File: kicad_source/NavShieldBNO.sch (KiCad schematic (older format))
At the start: 3 parts

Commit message: updated schematic, added schematic pdf
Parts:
- added C? (x5): 100nF, capacitors:C_0603, symbol devices:C_0603
- added R? (x11): DNI, resistors:R_0603, symbol devices:R_0603
- added R? (x9): 0R, resistors:R_0603, symbol devices:R_0603
- added R? (x5): 10k, resistors:R_0603, symbol devices:R_0603
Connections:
- net labels added: BNO085_CS, BNO085_INT, BOOTN, CAP, CLKSEL0, CSB, ENV_SCL, ENV_SDA, PS0, PS1, RESET, SCK, SDI, SDO
- wire segments 34 -> 128
- no-connect marks 3 -> 18
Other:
- note added: "i2c address 0x4A or 0x4B"
- note added: "i2c address 0x76 or 0x77"
- note added: "set to SPI"
- note added: "should also support BNO055, BNO070, BNO080 and BNO085\nas all have the same footprint and pin out"
- note added: "use internal clock"
- moved on the sheet: U?

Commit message: annotated schematic
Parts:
- gave numbers to parts that had none: 33

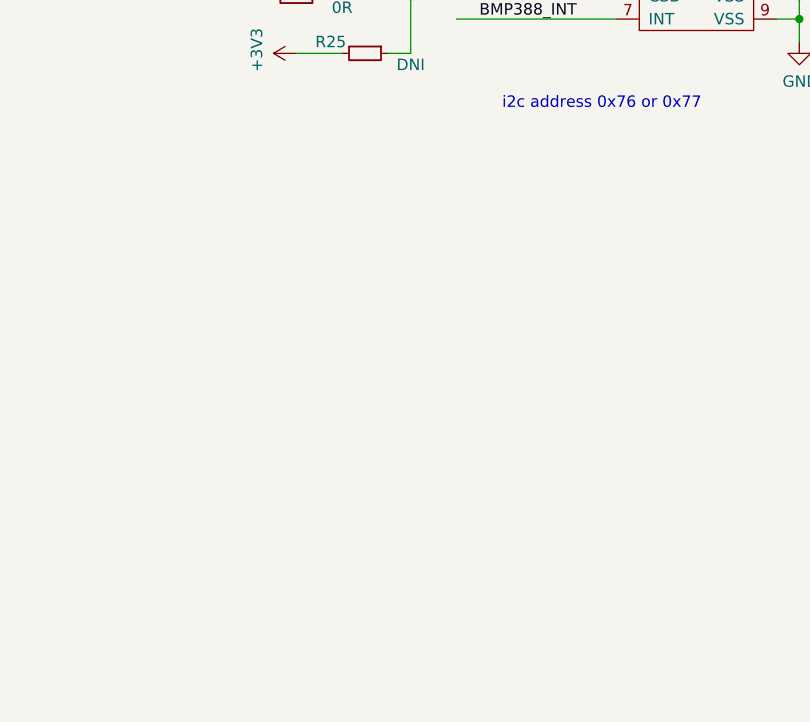
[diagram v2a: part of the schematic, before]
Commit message: added pull up on INT and reset lines
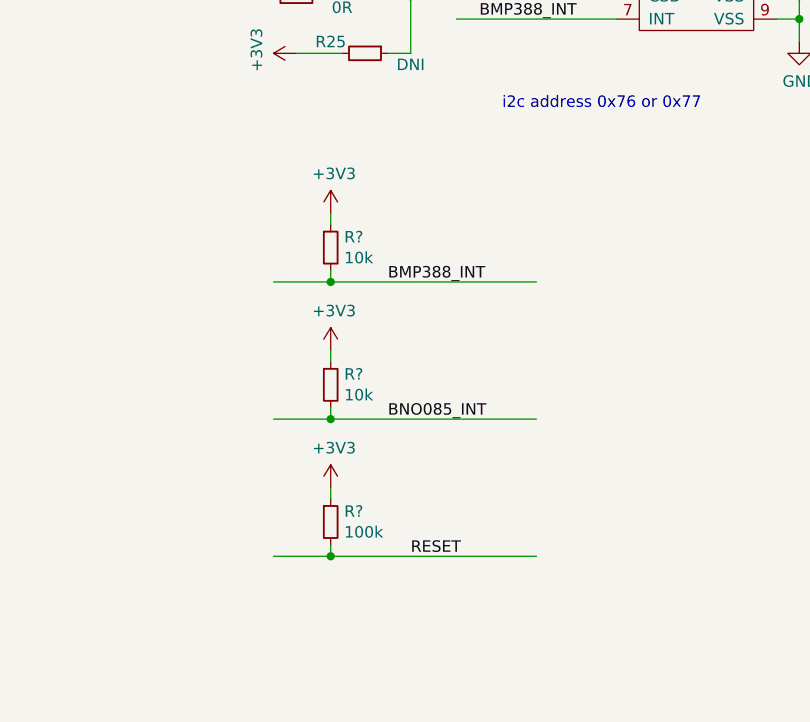
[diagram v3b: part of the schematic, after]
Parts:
- added R? (x2): 10k, resistors:R_0603, symbol devices:R_0603
- added R?: 100k, resistors:R_0603, symbol devices:R_0603
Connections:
- wire segments 128 -> 140
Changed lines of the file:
@@
 Text Notes 1900 700  0    50   ~ 0
 should also support BNO055, BNO070, BNO080 and BNO085\nas all have the same footprint and pin out
+$Comp
+L devices:R_0603 R?
+U 1 1 5F58EB42
+P 8950 3500
+F 0 "R?" H 9009 3546 50  0000 L CNN
+F 1 "10k" H 9009 3455 50  0000 L CNN
+F 2 "resistors:R_0603" H 8950 3350 50  0001 C CNN
+F 3 "" H 8950 3500 50  0000 C CNN
+	1    8950 3500
+	1    0    0    -1
+$EndComp
+$Comp
+L power-supply:+3V3 #PWR?
+U 1 1 5F58EB4C
+P 8950 3350
+F 0 "#PWR?" H 8950 3200 50  0001 C CNN
+F 1 "+3V3" H 8965 3523 50  0000 C CNN
+F 2 "" H 8950 3350 50  0000 C CNN
+F 3 "" H 8950 3350 50  0000 C CNN
+	1    8950 3350
+	1    0    0    -1
+$EndComp
+Wire Wire Line
+	8950 3350 8950 3400
+Wire Wire Line
+	8700 3650 8950 3650
+Wire Wire Line
+	8950 3600 8950 3650
+Connection ~ 8950 3650
+Wire Wire Line
+	8950 3650 9850 3650
+Text Label 9200 3650 0    50   ~ 0
+BMP388_INT
+$Comp
+L devices:R_0603 R?
+U 1 1 5F5A6A36
+P 8950 4100
+F 0 "R?" H 9009 4146 50  0000 L CNN
+F 1 "10k" H 9009 4055 50  0000 L CNN
+F 2 "resistors:R_0603" H 8950 3950 50  0001 C CNN
+F 3 "" H 8950 4100 50  0000 C CNN
+	1    8950 4100
+	1    0    0    -1
+$EndComp
+$Comp
+L power-supply:+3V3 #PWR?
+U 1 1 5F5A6A40
+P 8950 3950
+F 0 "#PWR?" H 8950 3800 50  0001 C CNN
+F 1 "+3V3" H 8965 4123 50  0000 C CNN
+F 2 "" H 8950 3950 50  0000 C CNN
+F 3 "" H 8950 3950 50  0000 C CNN
+	1    8950 3950
+	1    0    0    -1
+$EndComp
+Wire Wire Line
+	8950 3950 8950 4000
+Wire Wire Line
+	8700 4250 8950 4250
+Wire Wire Line
+	8950 4200 8950 4250
+Connection ~ 8950 4250
+Wire Wire Line
+	8950 4250 9850 4250
+Text Label 9200 4250 0    50   ~ 0
+BNO085_INT
+$Comp
+L devices:R_0603 R?
+U 1 1 5F5B49FC
+P 8950 4700
+F 0 "R?" H 9009 4746 50  0000 L CNN
+F 1 "100k" H 9009 4655 50  0000 L CNN
+F 2 "resistors:R_0603" H 8950 4550 50  0001 C CNN
+F 3 "" H 8950 4700 50  0000 C CNN
+	1    8950 4700
+	1    0    0    -1
+$EndComp
+$Comp
+L power-supply:+3V3 #PWR?
+U 1 1 5F5B4A06
+P 8950 4550
+F 0 "#PWR?" H 8950 4400 50  0001 C CNN
+F 1 "+3V3" H 8965 4723 50  0000 C CNN
+F 2 "" H 8950 4550 50  0000 C CNN
+F 3 "" H 8950 4550 50  0000 C CNN
+	1    8950 4550
+	1    0    0    -1
+$EndComp
+Wire Wire Line
+	8950 4550 8950 4600
+Wire Wire Line
+	8700 4850 8950 4850
+Wire Wire Line
+	8950 4800 8950 4850
+Connection ~ 8950 4850
+Wire Wire Line
+	8950 4850 9850 4850
+Text Label 9300 4850 0    50   ~ 0
+RESET
 $EndSCHEMATC

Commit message: connected CLKSEL1 to GND via resistor
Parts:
- added R?: 0R, resistors:R_0603, symbol devices:R_0603
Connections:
- net labels added: CLKSEL1
- wire segments 140 -> 142
- no-connect marks 18 -> 17
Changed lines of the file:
@@
 Text Label 2950 7100 0    50   ~ 0
 BNO085_CS
-NoConn ~ 4150 1800
 NoConn ~ 4150 1300
 Wire Wire Line
@@
 Text Label 9300 4850 0    50   ~ 0
 RESET
+$Comp
+L power-supply:GND #PWR?
+U 1 1 5F5C11F4
+P 4950 1800
+F 0 "#PWR?" H 4950 1550 50  0001 C CNN
+F 1 "GND" H 4955 1627 50  0000 C CNN
+F 2 "" H 4950 1800 50  0000 C CNN
+F 3 "" H 4950 1800 50  0000 C CNN
+	1    4950 1800
+	1    0    0    -1
+$EndComp
+$Comp
+L devices:R_0603 R?
+U 1 1 5F5C376C
+P 4750 1800
+F 0 "R?" H 4809 1846 50  0000 L CNN
+F 1 "0R" H 4809 1755 50  0000 L CNN
+F 2 "resistors:R_0603" H 4750 1650 50  0001 C CNN
+F 3 "" H 4750 1800 50  0000 C CNN
+	1    4750 1800
+	0    -1   -1   0
+$EndComp
+Wire Wire Line
+	4150 1800 4650 1800
+Wire Wire Line
+	4850 1800 4950 1800
+Text Label 4250 1800 0    50   ~ 0
+CLKSEL1
 $EndSCHEMATC

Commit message: moved BNO085_CS to D5, updated schematic pdf
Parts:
- gave numbers to parts that had none: 4
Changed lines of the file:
@@
 Wire Wire Line
 	4150 2750 5650 2750
-Wire Wire Line
-	2800 7100 3650 7100
-Text Label 2950 7100 0    50   ~ 0
+Text Label 2950 7300 0    50   ~ 0
 BNO085_CS
 NoConn ~ 4150 1300
@@
 NoConn ~ 4850 6500
 NoConn ~ 4850 6600
-NoConn ~ 3650 7300
 NoConn ~ 3650 7200
 NoConn ~ 3650 6900
@@
 should also support BNO055, BNO070, BNO080 and BNO085\nas all have the same footprint and pin out
 $Comp
-L devices:R_0603 R?
+L devices:R_0603 R27
 U 1 1 5F58EB42
 P 8950 3500
-F 0 "R?" H 9009 3546 50  0000 L CNN
+F 0 "R27" H 9009 3546 50  0000 L CNN
 F 1 "10k" H 9009 3455 50  0000 L CNN
 F 2 "resistors:R_0603" H 8950 3350 50  0001 C CNN
@@
 $EndComp
 $Comp
-L power-supply:+3V3 #PWR?
+L power-supply:+3V3 #PWR030
 U 1 1 5F58EB4C
 P 8950 3350
-F 0 "#PWR?" H 8950 3200 50  0001 C CNN
+F 0 "#PWR030" H 8950 3200 50  0001 C CNN
 F 1 "+3V3" H 8965 3523 50  0000 C CNN
 F 2 "" H 8950 3350 50  0000 C CNN
@@
 BMP388_INT
 $Comp
-L devices:R_0603 R?
+L devices:R_0603 R28
 U 1 1 5F5A6A36
 P 8950 4100
-F 0 "R?" H 9009 4146 50  0000 L CNN
+F 0 "R28" H 9009 4146 50  0000 L CNN
 F 1 "10k" H 9009 4055 50  0000 L CNN
 F 2 "resistors:R_0603" H 8950 3950 50  0001 C CNN
@@
 $EndComp
 $Comp
-L power-supply:+3V3 #PWR?
+L power-supply:+3V3 #PWR031
 U 1 1 5F5A6A40
 P 8950 3950
-F 0 "#PWR?" H 8950 3800 50  0001 C CNN
+F 0 "#PWR031" H 8950 3800 50  0001 C CNN
 F 1 "+3V3" H 8965 4123 50  0000 C CNN
 F 2 "" H 8950 3950 50  0000 C CNN
@@
 BNO085_INT
 $Comp
-L devices:R_0603 R?
+L devices:R_0603 R29
 U 1 1 5F5B49FC
 P 8950 4700
-F 0 "R?" H 9009 4746 50  0000 L CNN
+F 0 "R29" H 9009 4746 50  0000 L CNN
 F 1 "100k" H 9009 4655 50  0000 L CNN
 F 2 "resistors:R_0603" H 8950 4550 50  0001 C CNN
@@
 $EndComp
 $Comp
-L power-supply:+3V3 #PWR?
+L power-supply:+3V3 #PWR032
 U 1 1 5F5B4A06
 P 8950 4550
-F 0 "#PWR?" H 8950 4400 50  0001 C CNN
+F 0 "#PWR032" H 8950 4400 50  0001 C CNN
 F 1 "+3V3" H 8965 4723 50  0000 C CNN
 F 2 "" H 8950 4550 50  0000 C CNN
@@
 RESET
 $Comp
-L power-supply:GND #PWR?
+L power-supply:GND #PWR029
 U 1 1 5F5C11F4
 P 4950 1800
-F 0 "#PWR?" H 4950 1550 50  0001 C CNN
+F 0 "#PWR029" H 4950 1550 50  0001 C CNN
 F 1 "GND" H 4955 1627 50  0000 C CNN
 F 2 "" H 4950 1800 50  0000 C CNN
@@
 $EndComp
 $Comp
-L devices:R_0603 R?
+L devices:R_0603 R26
 U 1 1 5F5C376C
 P 4750 1800
-F 0 "R?" H 4809 1846 50  0000 L CNN
+F 0 "R26" H 4809 1846 50  0000 L CNN
 F 1 "0R" H 4809 1755 50  0000 L CNN
 F 2 "resistors:R_0603" H 4750 1650 50  0001 C CNN
@@
 Text Label 4250 1800 0    50   ~ 0
 CLKSEL1
+Wire Wire Line
+	2800 7300 3650 7300
+NoConn ~ 3650 7100
 $EndSCHEMATC

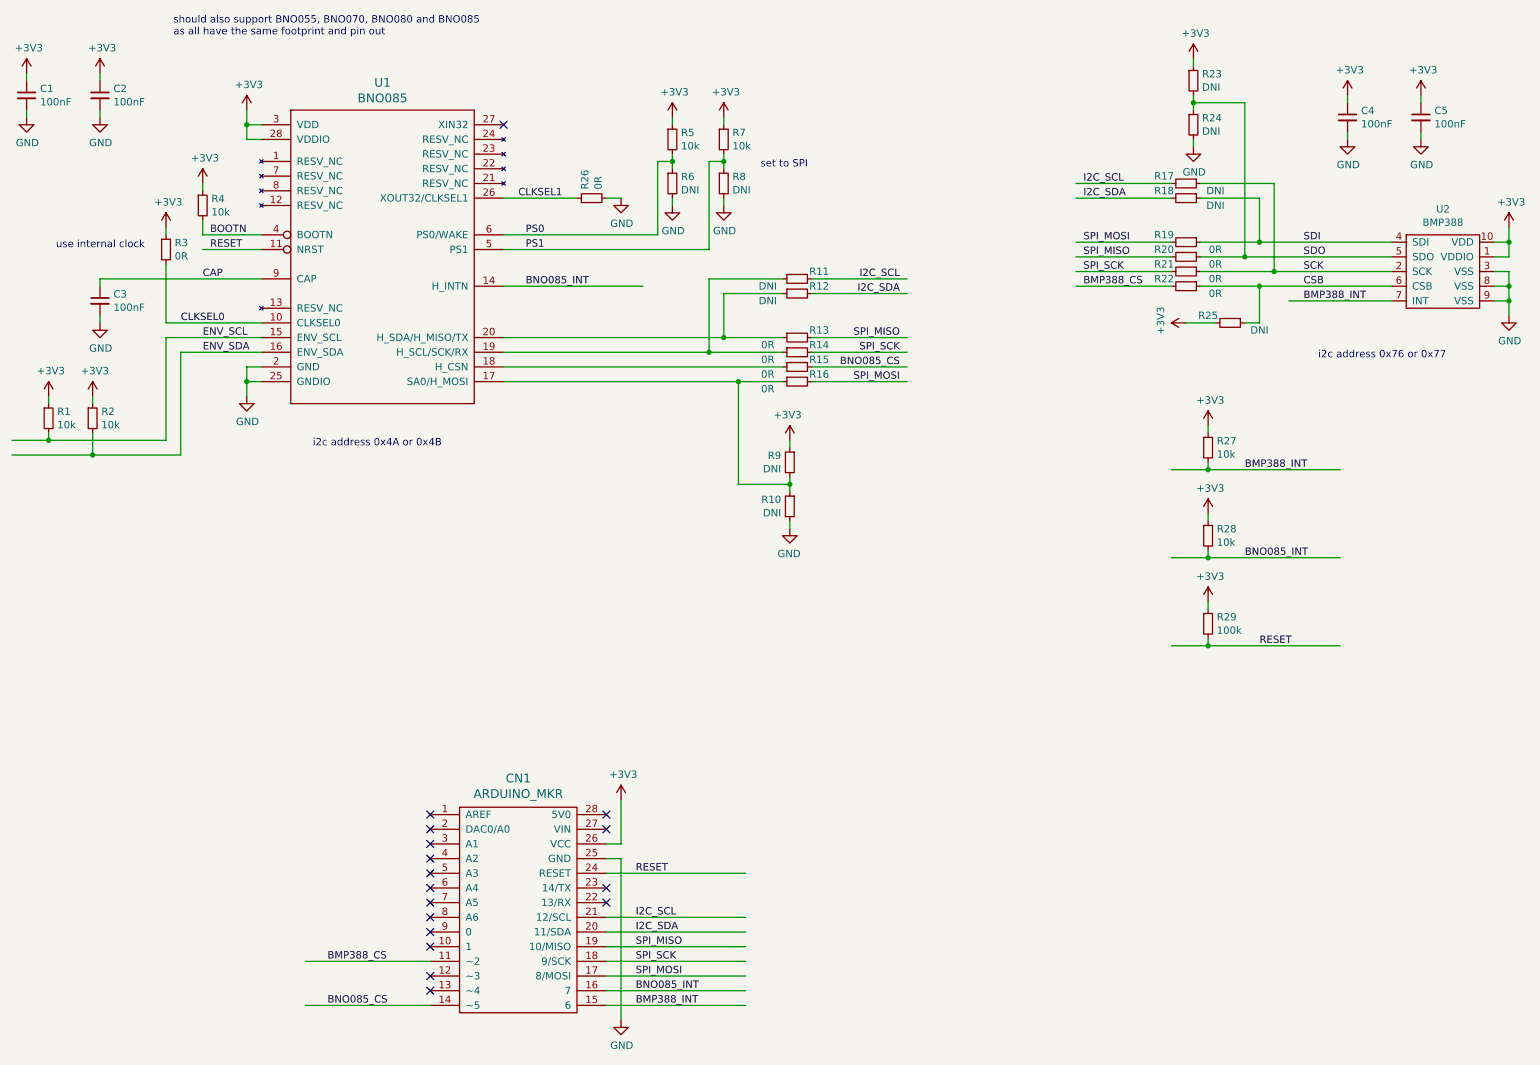
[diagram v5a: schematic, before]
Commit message: added WAKE signal to Arduino connector
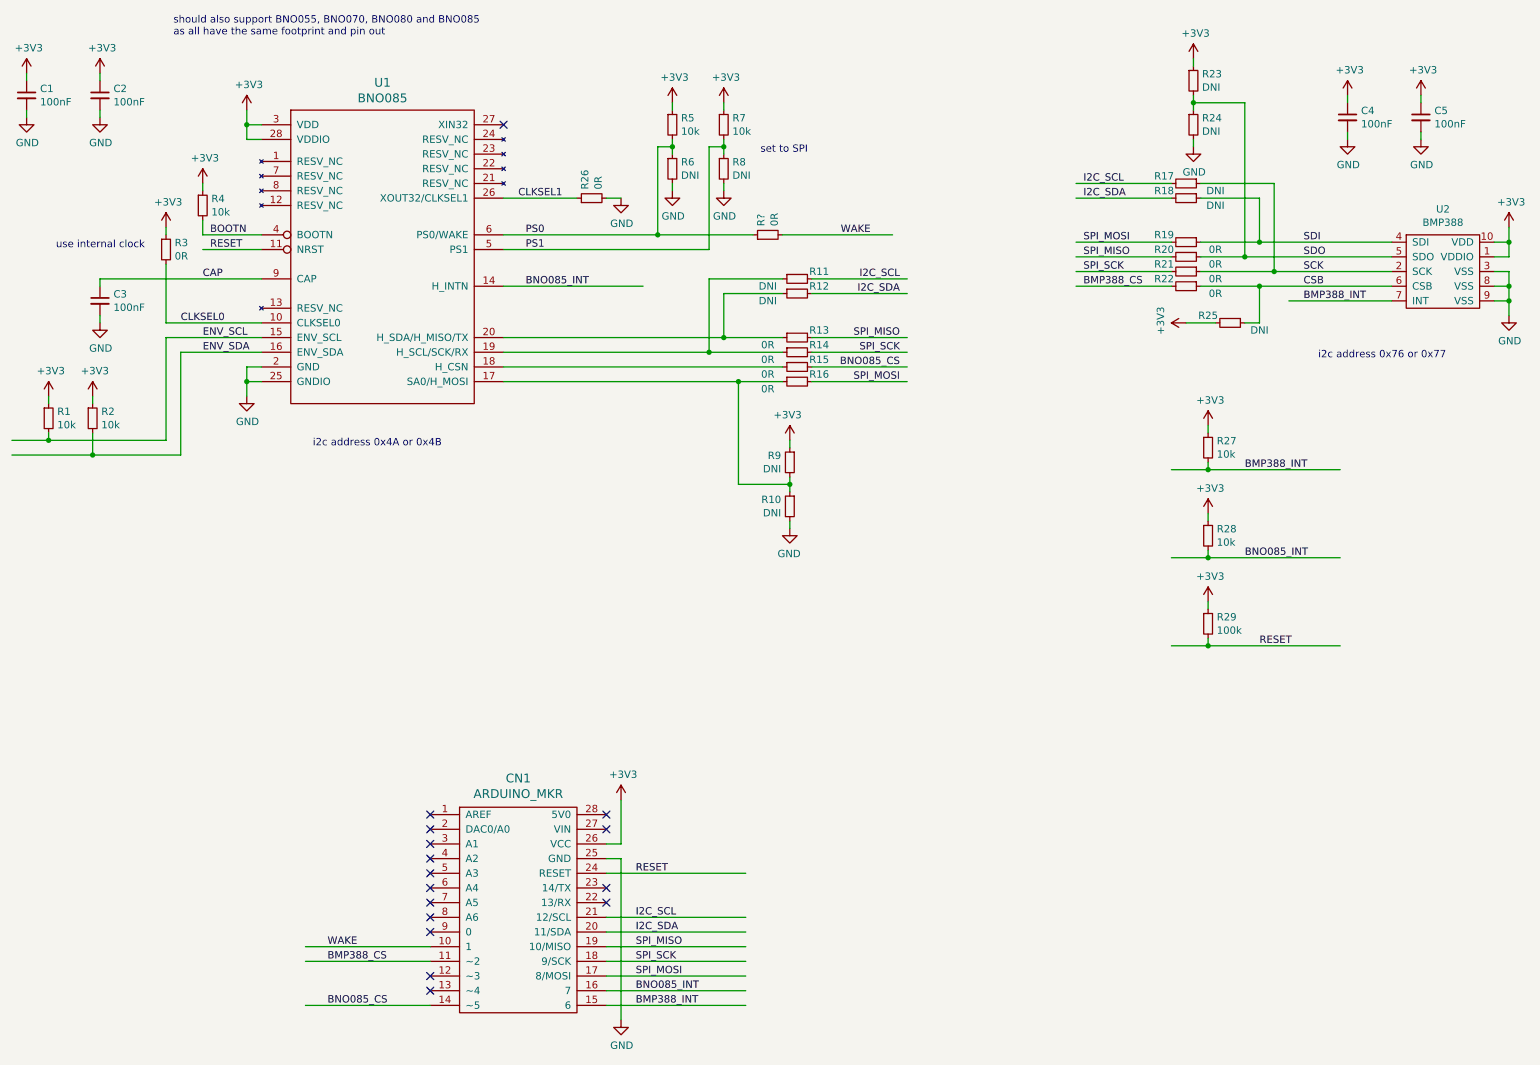
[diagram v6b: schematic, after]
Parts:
- added R?: 0R, resistors:R_0603, symbol devices:R_0603
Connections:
- net labels added: WAKE
- wire segments 142 -> 145
- no-connect marks 17 -> 16
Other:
- moved on the sheet: R5, R6, R7, R8
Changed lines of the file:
@@
 Sheet 1 1
 Title "NavShieldBNO"
-Date "2020-09-07"
+Date "2020-09-17"
 Rev "dev_0.1"
 Comp "generationmake"
@@
 L devices:R_0603 R5
 U 1 1 5F573F29
-P 5300 1400
-F 0 "R5" H 5359 1446 50  0000 L CNN
-F 1 "10k" H 5359 1355 50  0000 L CNN
-F 2 "resistors:R_0603" H 5300 1250 50  0001 C CNN
-F 3 "" H 5300 1400 50  0000 C CNN
-	1    5300 1400
+P 5300 1300
+F 0 "R5" H 5359 1346 50  0000 L CNN
+F 1 "10k" H 5359 1255 50  0000 L CNN
+F 2 "resistors:R_0603" H 5300 1150 50  0001 C CNN
+F 3 "" H 5300 1300 50  0000 C CNN
+	1    5300 1300
 	1    0    0    -1
 $EndComp
@@
 L devices:R_0603 R6
 U 1 1 5F574211
-P 5300 1700
-F 0 "R6" H 5359 1746 50  0000 L CNN
-F 1 "DNI" H 5359 1655 50  0000 L CNN
-F 2 "resistors:R_0603" H 5300 1550 50  0001 C CNN
-F 3 "" H 5300 1700 50  0000 C CNN
-	1    5300 1700
+P 5300 1600
+F 0 "R6" H 5359 1646 50  0000 L CNN
+F 1 "DNI" H 5359 1555 50  0000 L CNN
+F 2 "resistors:R_0603" H 5300 1450 50  0001 C CNN
+F 3 "" H 5300 1600 50  0000 C CNN
+	1    5300 1600
 	1    0    0    -1
 $EndComp
@@
 L power-supply:+3V3 #PWR014
 U 1 1 5F574583
-P 5300 1250
-F 0 "#PWR014" H 5300 1100 50  0001 C CNN
-F 1 "+3V3" H 5315 1423 50  0000 C CNN
-F 2 "" H 5300 1250 50  0000 C CNN
-F 3 "" H 5300 1250 50  0000 C CNN
-	1    5300 1250
+P 5300 1150
+F 0 "#PWR014" H 5300 1000 50  0001 C CNN
+F 1 "+3V3" H 5315 1323 50  0000 C CNN
+F 2 "" H 5300 1150 50  0000 C CNN
+F 3 "" H 5300 1150 50  0000 C CNN
+	1    5300 1150
 	1    0    0    -1
 $EndComp
@@
 L power-supply:GND #PWR015
 U 1 1 5F5748FA
-P 5300 1850
-F 0 "#PWR015" H 5300 1600 50  0001 C CNN
-F 1 "GND" H 5305 1677 50  0000 C CNN
-F 2 "" H 5300 1850 50  0000 C CNN
-F 3 "" H 5300 1850 50  0000 C CNN
-	1    5300 1850
-	1    0    0    -1
-$EndComp
-Wire Wire Line
-	5300 1250 5300 1300
-Wire Wire Line
-	5300 1500 5300 1550
-Wire Wire Line
-	5300 1800 5300 1850
+P 5300 1750
+F 0 "#PWR015" H 5300 1500 50  0001 C CNN
+F 1 "GND" H 5305 1577 50  0000 C CNN
+F 2 "" H 5300 1750 50  0000 C CNN
+F 3 "" H 5300 1750 50  0000 C CNN
+	1    5300 1750
+	1    0    0    -1
+$EndComp
+Wire Wire Line
+	5300 1150 5300 1200
+Wire Wire Line
+	5300 1400 5300 1450
+Wire Wire Line
+	5300 1700 5300 1750
 $Comp
 L devices:R_0603 R7
 U 1 1 5F57A796
-P 5650 1400
-F 0 "R7" H 5709 1446 50  0000 L CNN
-F 1 "10k" H 5709 1355 50  0000 L CNN
-F 2 "resistors:R_0603" H 5650 1250 50  0001 C CNN
-F 3 "" H 5650 1400 50  0000 C CNN
-	1    5650 1400
+P 5650 1300
+F 0 "R7" H 5709 1346 50  0000 L CNN
+F 1 "10k" H 5709 1255 50  0000 L CNN
+F 2 "resistors:R_0603" H 5650 1150 50  0001 C CNN
+F 3 "" H 5650 1300 50  0000 C CNN
+	1    5650 1300
 	1    0    0    -1
 $EndComp
@@
 L devices:R_0603 R8
 U 1 1 5F57A7A0
-P 5650 1700
-F 0 "R8" H 5709 1746 50  0000 L CNN
-F 1 "DNI" H 5709 1655 50  0000 L CNN
-F 2 "resistors:R_0603" H 5650 1550 50  0001 C CNN
-F 3 "" H 5650 1700 50  0000 C CNN
-	1    5650 1700
+P 5650 1600
+F 0 "R8" H 5709 1646 50  0000 L CNN
+F 1 "DNI" H 5709 1555 50  0000 L CNN
+F 2 "resistors:R_0603" H 5650 1450 50  0001 C CNN
+F 3 "" H 5650 1600 50  0000 C CNN
+	1    5650 1600
 	1    0    0    -1
 $EndComp
@@
 L power-supply:+3V3 #PWR016
 U 1 1 5F57A7AA
-P 5650 1250
-F 0 "#PWR016" H 5650 1100 50  0001 C CNN
-F 1 "+3V3" H 5665 1423 50  0000 C CNN
-F 2 "" H 5650 1250 50  0000 C CNN
-F 3 "" H 5650 1250 50  0000 C CNN
-	1    5650 1250
+P 5650 1150
+F 0 "#PWR016" H 5650 1000 50  0001 C CNN
+F 1 "+3V3" H 5665 1323 50  0000 C CNN
+F 2 "" H 5650 1150 50  0000 C CNN
+F 3 "" H 5650 1150 50  0000 C CNN
+	1    5650 1150
 	1    0    0    -1
 $EndComp
@@
 L power-supply:GND #PWR017
 U 1 1 5F57A7B4
-P 5650 1850
-F 0 "#PWR017" H 5650 1600 50  0001 C CNN
-F 1 "GND" H 5655 1677 50  0000 C CNN
-F 2 "" H 5650 1850 50  0000 C CNN
-F 3 "" H 5650 1850 50  0000 C CNN
-	1    5650 1850
-	1    0    0    -1
-$EndComp
-Wire Wire Line
-	5650 1250 5650 1300
-Wire Wire Line
-	5650 1500 5650 1550
-Wire Wire Line
-	5650 1800 5650 1850
+P 5650 1750
+F 0 "#PWR017" H 5650 1500 50  0001 C CNN
+F 1 "GND" H 5655 1577 50  0000 C CNN
+F 2 "" H 5650 1750 50  0000 C CNN
+F 3 "" H 5650 1750 50  0000 C CNN
+	1    5650 1750
+	1    0    0    -1
+$EndComp
+Wire Wire Line
+	5650 1150 5650 1200
+Wire Wire Line
+	5650 1400 5650 1450
+Wire Wire Line
+	5650 1700 5650 1750
 Wire Wire Line
 	4150 2150 5550 2150
 Wire Wire Line
-	5550 2150 5550 1550
-Wire Wire Line
-	5550 1550 5650 1550
-Connection ~ 5650 1550
-Wire Wire Line
-	5650 1550 5650 1600
-Wire Wire Line
-	5200 2050 5200 1550
-Wire Wire Line
-	5200 1550 5300 1550
-Connection ~ 5300 1550
-Wire Wire Line
-	5300 1550 5300 1600
+	5550 1450 5650 1450
+Connection ~ 5650 1450
+Wire Wire Line
+	5650 1450 5650 1500
+Wire Wire Line
+	5200 1450 5300 1450
+Connection ~ 5300 1450
+Wire Wire Line
+	5300 1450 5300 1500
 Wire Wire Line
 	4150 2050 5200 2050
@@
 Text Label 4300 2150 0    50   ~ 0
 PS1
-Text Notes 5900 1600 0    50   ~ 0
+Text Notes 5900 1500 0    50   ~ 0
 set to SPI
 $Comp
@@
 NoConn ~ 4850 6600
 NoConn ~ 3650 7200
-NoConn ~ 3650 6900
 NoConn ~ 3650 6800
 NoConn ~ 3650 6700
@@
 	2800 7300 3650 7300
 NoConn ~ 3650 7100
+Wire Wire Line
+	5200 1450 5200 2050
+Wire Wire Line
+	5550 1450 5550 2150
+$Comp
+L devices:R_0603 R?
+U 1 1 5F6453B8
+P 5950 2050
+F 0 "R?" H 6009 2096 50  0000 L CNN
+F 1 "0R" H 6009 2005 50  0000 L CNN
+F 2 "resistors:R_0603" H 5950 1900 50  0001 C CNN
+F 3 "" H 5950 2050 50  0000 C CNN
+	1    5950 2050
+	0    -1   -1   0
+$EndComp
+Wire Wire Line
+	6800 2050 6050 2050
+Wire Wire Line
+	5850 2050 5200 2050
+Connection ~ 5200 2050
+Text Label 6650 2050 2    50   ~ 0
+WAKE
+Wire Wire Line
+	2800 6900 3650 6900
+Text Label 2950 6900 0    50   ~ 0
+WAKE
 $EndSCHEMATC
